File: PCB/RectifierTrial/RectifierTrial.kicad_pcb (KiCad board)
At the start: 2 copper layers, 9 parts, among them J1 Conn_01x03, J2 Conn_01x02

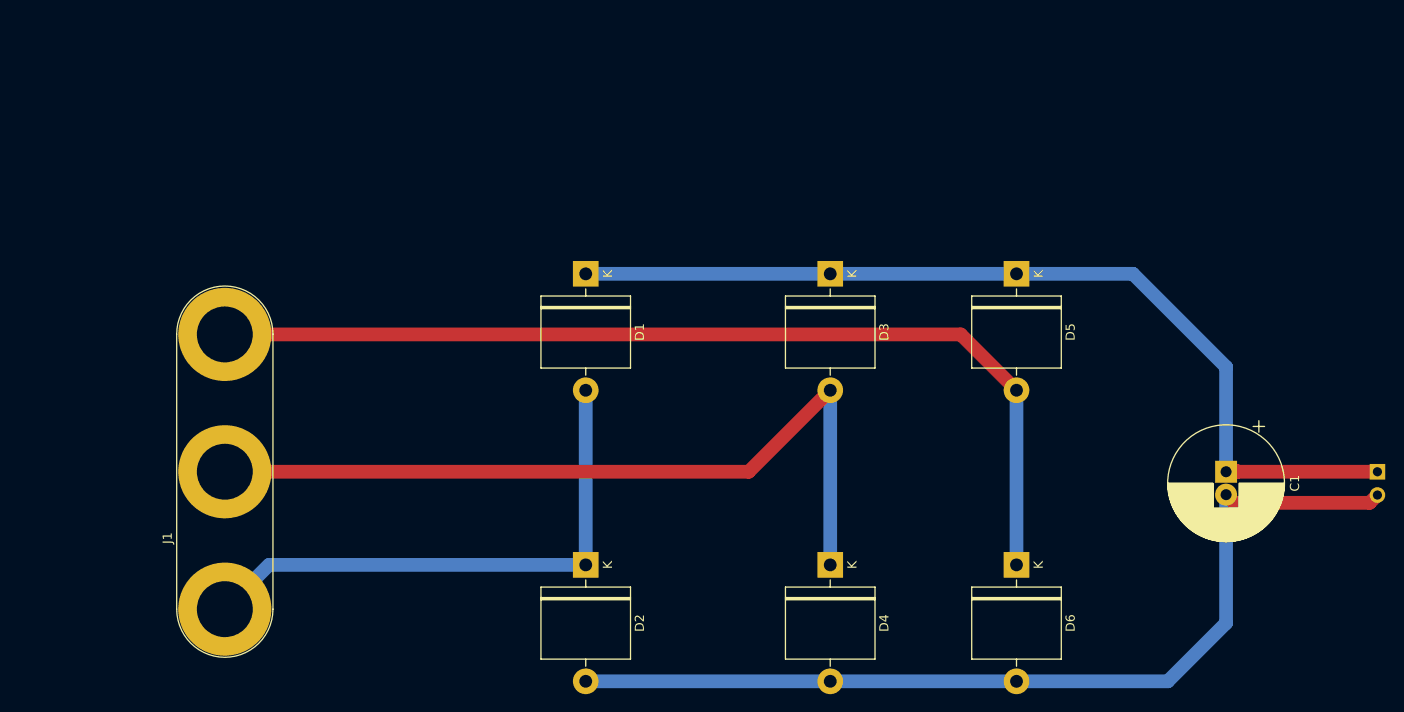
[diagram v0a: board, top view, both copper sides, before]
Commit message: Rectifier PCB is added
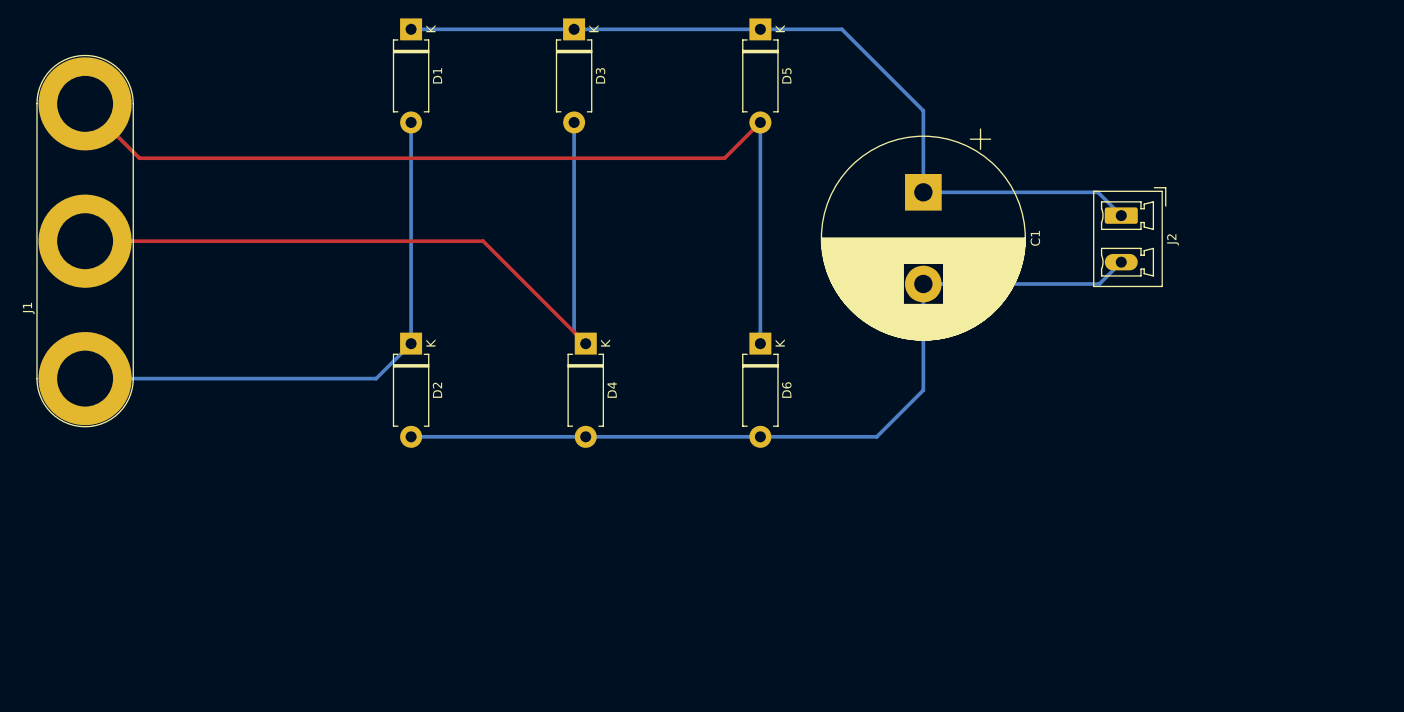
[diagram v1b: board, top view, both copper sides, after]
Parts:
- C1: value 0.004 -> 56uF; footprint Capacitor_THT:CP_Radial_D12.5mm_P2.50mm -> Capacitor_THT:CP_Radial_D22.0mm_P10.00mm_SnapIn
- D1, D2, D3, D4, D5, D6: footprint Diode_THT:D_5KP_P12.70mm_Horizontal -> Diode_THT:D_DO-15_P10.16mm_Horizontal
- J2: footprint Connector_PinSocket_2.54mm:PinSocket_1x02_P2.54mm_Horizontal -> Connector_Phoenix_MC_HighVoltage:PhoenixContact_MCV_1,5_2-G-5.08_1x02_P5.08mm_Vertical; moved to F.Cu
- moved C1 44.9 mm to (149.9, 71.1)
- moved J2 39.5 mm to (171.4, 73.7), turned to 270 degrees
- moved D5 38.6 mm to (132.1, 53.3)
- moved D3 38.6 mm to (111.8, 53.3)
- moved D6 36.9 mm to (132.1, 87.6)
- moved D4 36.0 mm to (113.0, 87.6)
- moved D1 32.8 mm to (94.0, 53.3)
- moved D2 30.7 mm to (94.0, 87.6)
- moved J1 29.4 mm to (58.4, 91.4)
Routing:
- net Net-(C1-Pad2): track 103.7 -> 92.2 mm
- net Net-(C1-Pad1): track 102.0 -> 91.1 mm
- net Net-(D5-Pad2): track 107.9 -> 101.9 mm
- net Net-(D3-Pad2): track 88.8 -> 83.9 mm
- net Net-(D1-Pad2): track 60.4 -> 61.3 mm
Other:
- net class Default: clearance 0.6 -> 2.5; trace_width 1.5 -> 0.4
- rule trace_clearance: 0.6 -> 2.5
